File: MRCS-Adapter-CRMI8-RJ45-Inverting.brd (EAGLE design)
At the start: 31 x 50 mm, 17 parts, among them CON1 CONNECTOR-M033.5MM-LOCK, J1 RJ45, M1 MOUNTINGHOLE, M2 MOUNTINGHOLE

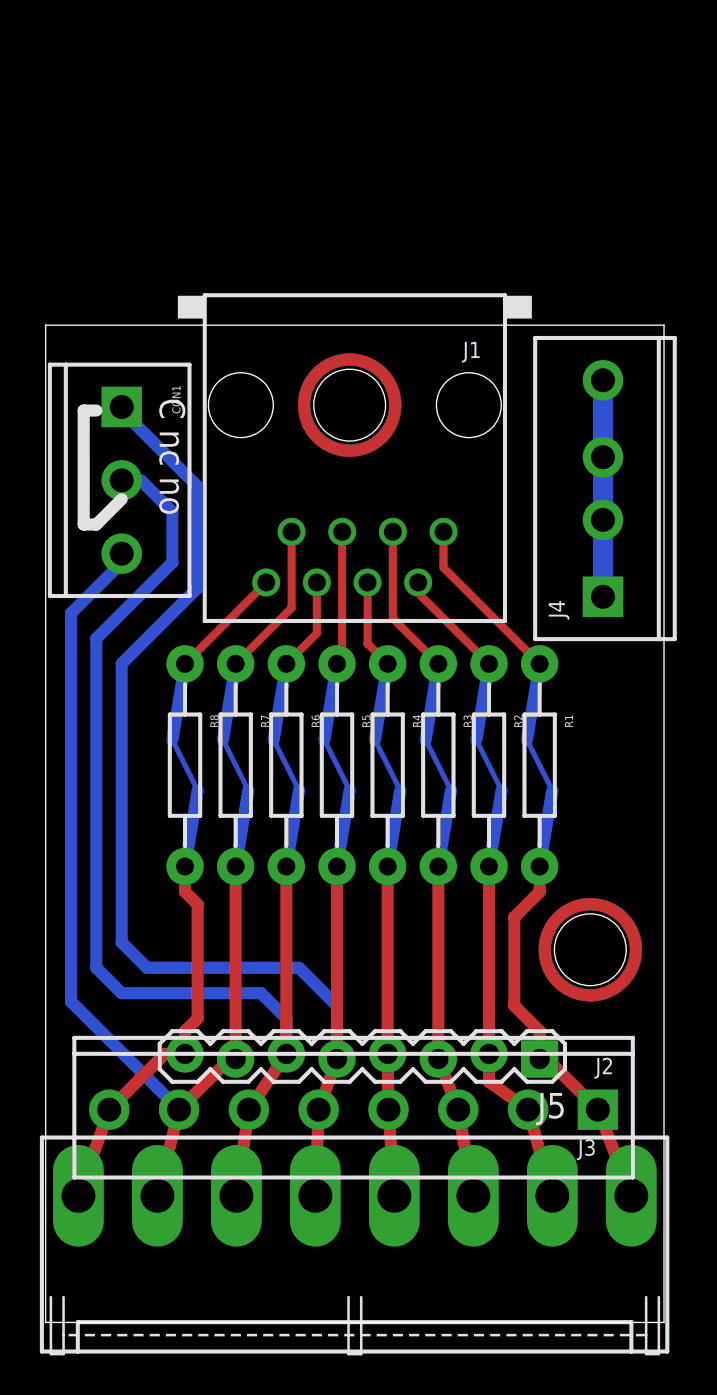
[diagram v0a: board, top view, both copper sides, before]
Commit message: added 74LS540, modified connectors
Added inverter (74LS540), removed frog connector, added Vcc, Gnd for logic supply
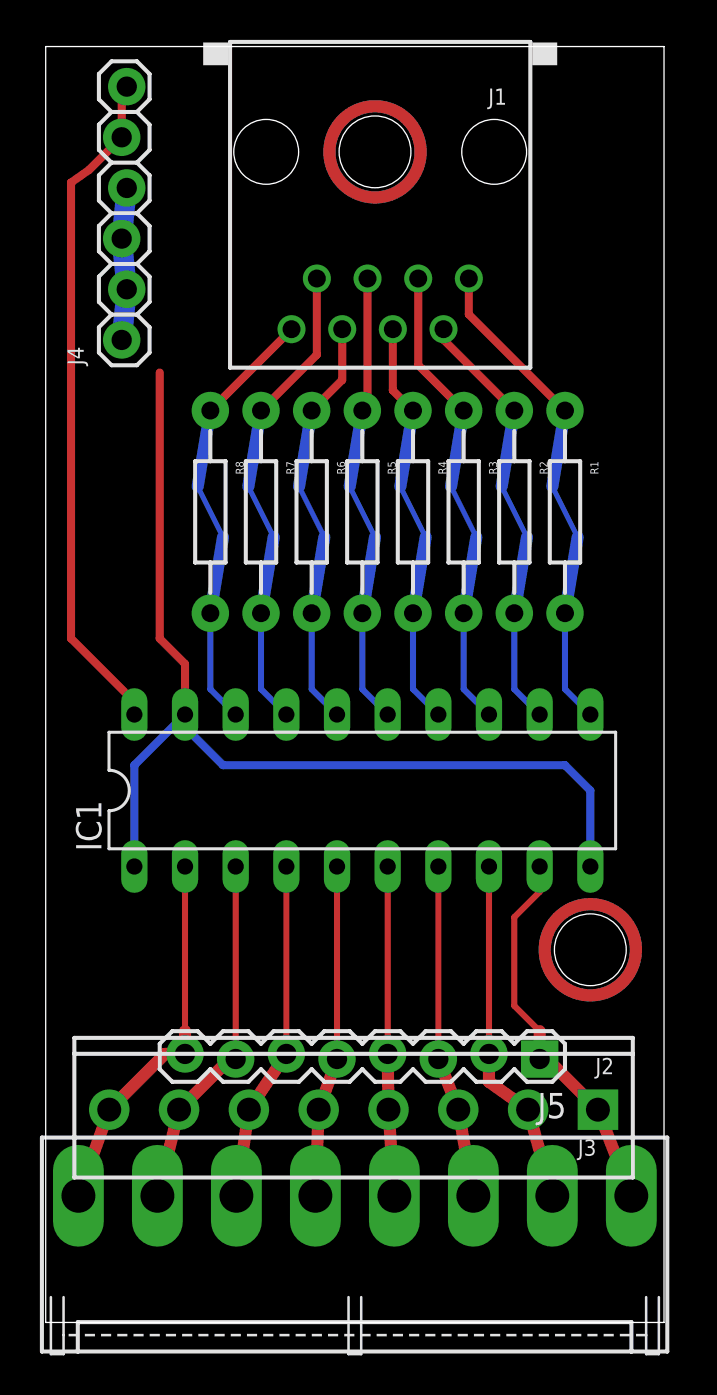
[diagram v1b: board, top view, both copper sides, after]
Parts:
- removed CON1: CONNECTOR-M033.5MM-LOCK, SPCoast:SCREWTERMINAL-3.5MM-3_LOCK.007S
- added IC1: 74LS540N, 74xx-us:DIL20
- J4: device SPCoast:SCREWTERMINAL-3.5MM-4_LOCK -> SPCoast:1X06_LOCK
- moved J4 27.3 mm to (3.81, 49.3)
- moved R1 12.8 mm to (26.0, 40.6)
- moved R2 12.8 mm to (23.5, 40.6)
- moved R3 12.8 mm to (21.0, 40.6)
- moved R4 12.8 mm to (18.4, 40.6)
- moved R5 12.8 mm to (15.9, 40.6)
- moved R6 12.8 mm to (13.3, 40.6)
- moved R7 12.8 mm to (10.8, 40.6)
- moved R8 12.8 mm to (8.26, 40.6)
- moved J1 12.8 mm to (16.8, 58.7)
- moved M1 12.8 mm to (16.5, 58.7)
- moved U$1 12.8 mm to (16.5, 58.7)
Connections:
- new net N$2: IC1.18, J1.8, R8.P$1, R8.P$2
- new net N$3: IC1.17, J1.7, R7.P$1, R7.P$2
- new net N$4: IC1.16, J1.6, R6.P$1, R6.P$2
- new net N$5: IC1.15, J1.5, R5.P$1, R5.P$2
- new net N$6: IC1.14, J1.4, R4.P$1, R4.P$2
- new net N$7: IC1.13, J1.3, R3.P$1, R3.P$2
- new net N$8: IC1.12, J1.2, R2.P$1, R2.P$2
- new net N$9: IC1.11, J1.1, R1.P$1, R1.P$2
- new net VCC: IC1.20, J4.5, J4.6
- net GND: now also IC1.1, IC1.10, IC1.19
- net L1: now also IC1.9; no longer J1.1, R1.P$1, R1.P$2
- net L2: now also IC1.8; no longer J1.2, R2.P$1, R2.P$2
- net L3: now also IC1.7; no longer J1.3, R3.P$1, R3.P$2
- net L4: now also IC1.6; no longer J1.4, R4.P$1, R4.P$2
- net L5: now also IC1.5; no longer CON1.1, J1.5, R5.P$1, R5.P$2
- net L6: now also IC1.4; no longer CON1.2, J1.6, R6.P$1, R6.P$2
- net L7: now also IC1.3; no longer CON1.3, J1.7, R7.P$1, R7.P$2
- net L8: now also IC1.2; no longer J1.8, R8.P$1, R8.P$2
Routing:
- net L5: track 78.7 -> 16.7 mm
- net L6: track 72.4 -> 17.1 mm
- net GND: track 10.9 -> 60.1 mm
- net L7: track 67.1 -> 18.0 mm
- net VCC: track 0.00 -> 34.0 mm
- net N$9: track 0.00 -> 24.8 mm
- net N$3: track 0.00 -> 24.0 mm
- net N$7: track 0.00 -> 23.7 mm
- net N$5: track 0.00 -> 22.9 mm
- net N$2: track 0.00 -> 21.9 mm
- net N$8: track 0.00 -> 21.7 mm
- net N$4: track 0.00 -> 20.9 mm
- net N$6: track 0.00 -> 20.7 mm
- net L1: track 38.5 -> 19.3 mm
- net L3: track 35.7 -> 17.1 mm
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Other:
- board size 31 x 50 mm -> 31 x 64 mm
- board text added: "2020.11"
- board text added: "VCC VCC GND GND GND GND"
- board text added: "v1.0"
- board text removed: "2020.06"
- board text removed: "C nc no"
- board text removed: "v5.0"
